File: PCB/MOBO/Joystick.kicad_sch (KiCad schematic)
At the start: 23 parts, among them J107 DTR, J107 MISO, J107 MOSI, J107 RXD, J107 SCK, J107 TXD, SW301 RS Button, SW302 LS Button, SW303 DPAD Right, SW304 DPAD Left, SW306 B Button, SW307 A Button, SW308 DPAD Down, SW309 DPAD Up, U301 ATmega328PB-M, Y301 YABM11-16.000MHZ-12-B1U-T

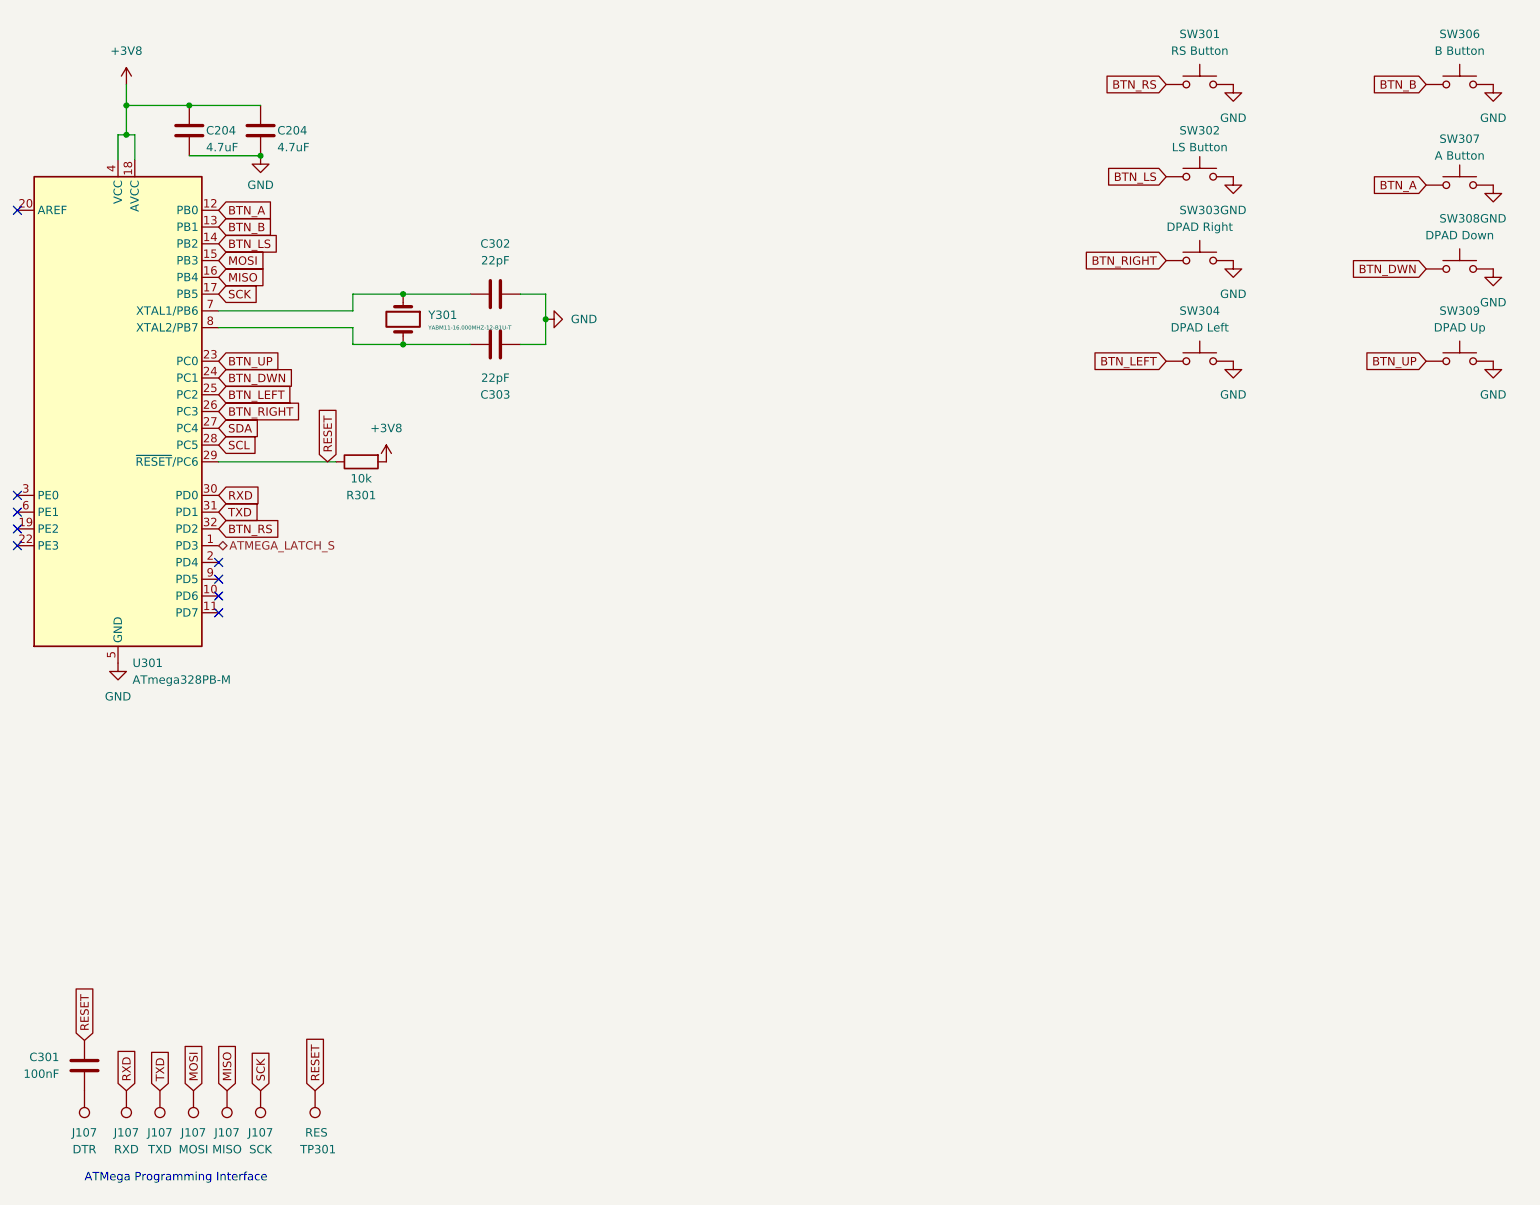
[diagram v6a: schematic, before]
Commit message: Started pcb traces
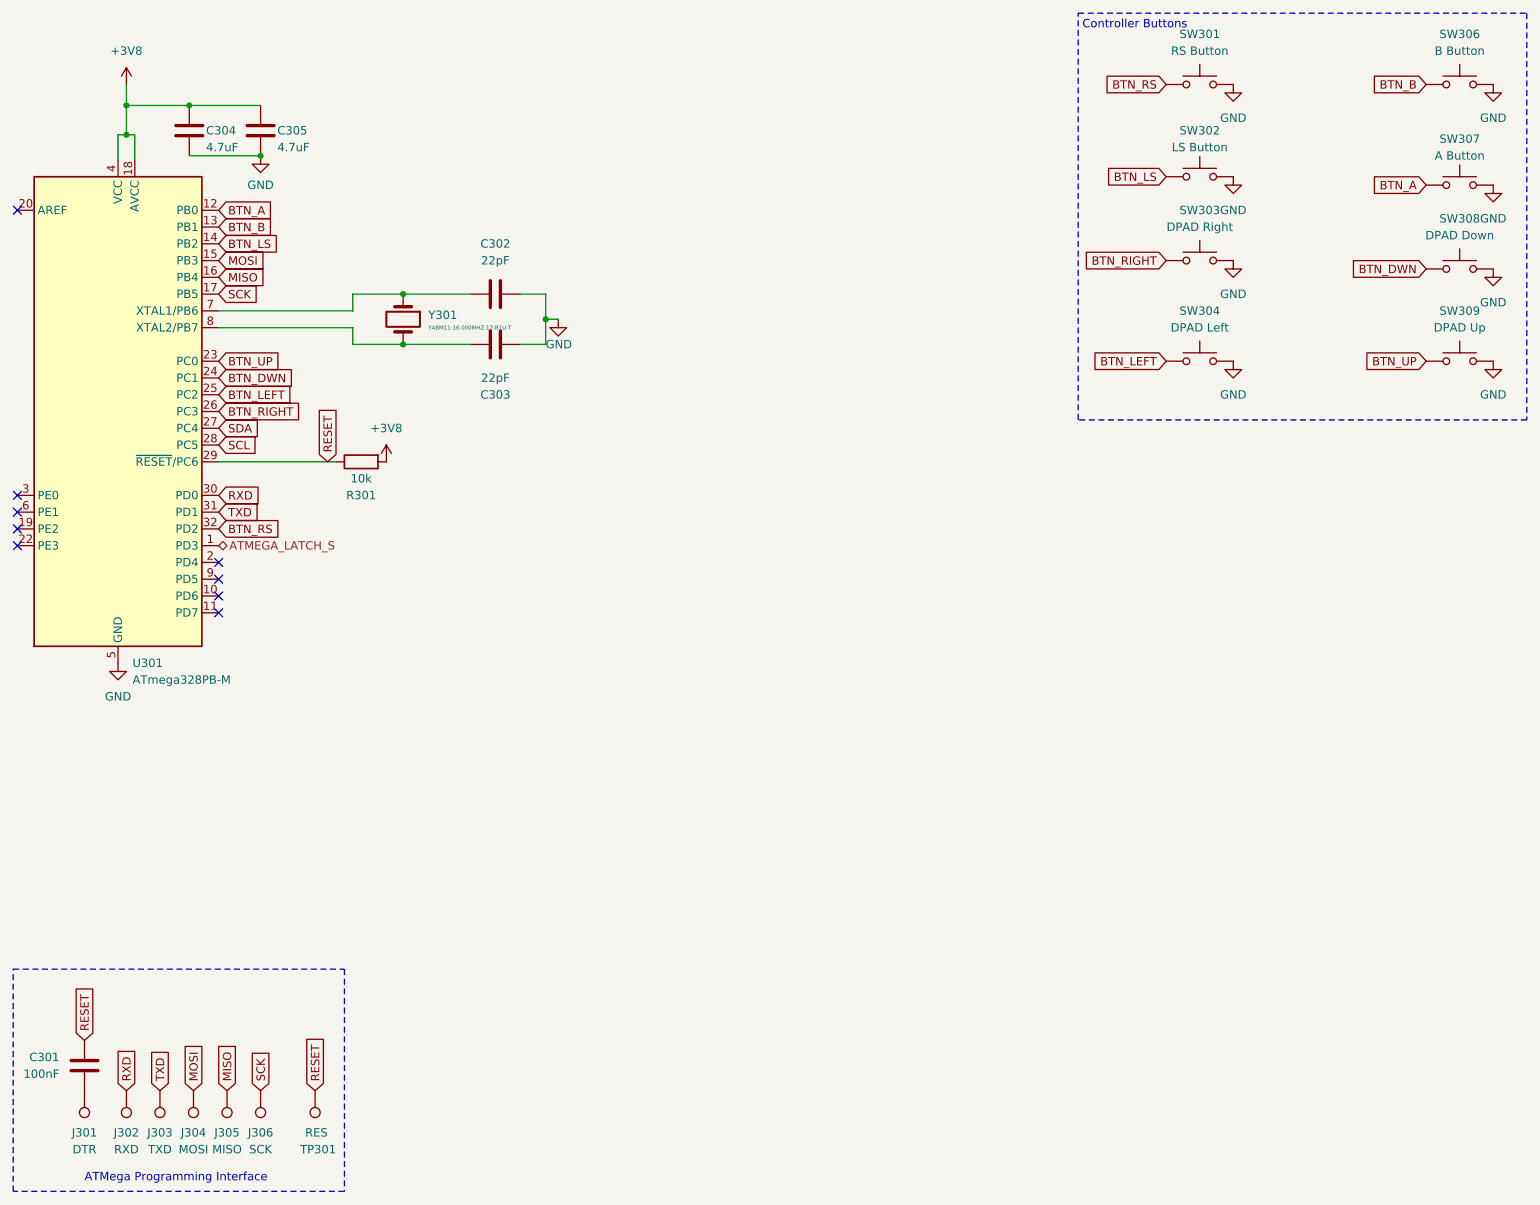
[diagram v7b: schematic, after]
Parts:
- renumbered C204 to C304, C204 to C305, J107 to J301, J107 to J302, J107 to J303, J107 to J304, J107 to J305, J107 to J306
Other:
- note added: "Controller Buttons"
- title: (none) -> ATMega & Buttons
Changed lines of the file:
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@@
 (kicad_sch (version 20230121) (generator eeschema)
   (paper "A4")
+  (title_block
+    (title "ATMega & Buttons")
+    (date "2023-06-06")
+    (rev "0.5")
+    (comment 1 "Repo: https://github.com/ilnerdchuck/GBA-SPi")
+  )
   (junction (at 78.74 64.77) (diameter 0) (color 0 0 0 0)
   )
@@
     (stroke (width 0) (type default))
   )
+  (wire (pts (xy 102.235 60.96) (xy 100.33 60.96))
+    (stroke (width 0) (type default))
+  )
   (wire (pts (xy 100.33 60.96) (xy 100.33 64.77))
     (stroke (width 0) (type default))
@@
     (stroke (width 0) (type default))
   )
+  (rectangle (start 180.975 14.605) (end 248.92 76.2)
+    (stroke (width 0) (type dash_dot_dot))
+    (fill (type none))
+  )
+  (rectangle (start 19.685 159.385) (end 69.85 193.04)
+    (stroke (width 0) (type dash_dot_dot))
+    (fill (type none))
+  )
   (text "ATMega Programming Interface\n" (at 30.48 191.77 0)
+    (effects (font (size 1.27 1.27)) (justify left bottom))
+  )
+  (text "Controller Buttons\n" (at 181.61 17.145 0)
     (effects (font (size 1.27 1.27)) (justify left bottom))
   )
@@
     )
   )
-  (symbol (lib_id "power:GND") (at 100.33 60.96 90) (unit 1)
-    (in_bom yes) (on_board yes) (dnp no) (fields_autoplaced)
-    (property "Reference" "#PWR0302" (at 106.68 60.96 0)
-      (effects (font (size 1.27 1.27)) hide)
-    )
-    (property "Value" "GND" (at 104.14 60.96 90)
-      (effects (font (size 1.27 1.27)) (justify right))
-    )
-    (property "Footprint" "" (at 100.33 60.96 0)
-      (effects (font (size 1.27 1.27)) hide)
-    )
-    (property "Datasheet" "" (at 100.33 60.96 0)
+  (symbol (lib_id "power:GND") (at 102.235 60.96 0) (unit 1)
+    (in_bom yes) (on_board yes) (dnp no)
+    (property "Reference" "#PWR0302" (at 102.235 67.31 0)
+      (effects (font (size 1.27 1.27)) hide)
+    )
+    (property "Value" "GND" (at 100.33 64.77 0)
+      (effects (font (size 1.27 1.27)) (justify left))
+    )
+    (property "Footprint" "" (at 102.235 60.96 0)
+      (effects (font (size 1.27 1.27)) hide)
+    )
+    (property "Datasheet" "" (at 102.235 60.96 0)
       (effects (font (size 1.27 1.27)) hide)
     )
@@
   (symbol (lib_id "Connector:TestPoint") (at 30.48 177.8 180) (unit 1)
     (in_bom yes) (on_board yes) (dnp no)
-    (property "Reference" "J107" (at 30.48 184.15 0)
+    (property "Reference" "J301" (at 30.48 184.15 0)
       (effects (font (size 1.27 1.27)))
     )
@@
     (instances
       (project "MOBO"
-        (path "/2d62a3c1-c4f2-4921-9f6b-8dc8aef69d64"
-          (reference "J107") (unit 1)
-        )
         (path "/2d62a3c1-c4f2-4921-9f6b-8dc8aef69d64/7ca0e1b4-2467-452a-8d82-c598e33fab6f"
           (reference "J301") (unit 1)
@@
   (symbol (lib_id "Device:C") (at 46.355 32.385 0) (unit 1)
     (in_bom yes) (on_board yes) (dnp no)
-    (property "Reference" "C204" (at 48.895 32.385 0)
+    (property "Reference" "C304" (at 48.895 32.385 0)
       (effects (font (size 1.27 1.27)) (justify left))
     )
@@
     (instances
       (project "MOBO"
-        (path "/2d62a3c1-c4f2-4921-9f6b-8dc8aef69d64/968b581c-59b8-4e39-ae9d-82f589704db7"
-          (reference "C204") (unit 1)
-        )
         (path "/2d62a3c1-c4f2-4921-9f6b-8dc8aef69d64/7ca0e1b4-2467-452a-8d82-c598e33fab6f"
           (reference "C304") (unit 1)
@@
   (symbol (lib_id "Connector:TestPoint") (at 57.15 177.8 180) (unit 1)
     (in_bom yes) (on_board yes) (dnp no)
-    (property "Reference" "J107" (at 57.15 184.15 0)
+    (property "Reference" "J306" (at 57.15 184.15 0)
       (effects (font (size 1.27 1.27)))
     )
@@
     (instances
       (project "MOBO"
-        (path "/2d62a3c1-c4f2-4921-9f6b-8dc8aef69d64"
-          (reference "J107") (unit 1)
-        )
         (path "/2d62a3c1-c4f2-4921-9f6b-8dc8aef69d64/7ca0e1b4-2467-452a-8d82-c598e33fab6f"
           (reference "J306") (unit 1)
@@
   (symbol (lib_id "Connector:TestPoint") (at 41.91 177.8 180) (unit 1)
     (in_bom yes) (on_board yes) (dnp no)
-    (property "Reference" "J107" (at 41.91 184.15 0)
+    (property "Reference" "J303" (at 41.91 184.15 0)
       (effects (font (size 1.27 1.27)))
     )
@@
     (instances
       (project "MOBO"
-        (path "/2d62a3c1-c4f2-4921-9f6b-8dc8aef69d64"
-          (reference "J107") (unit 1)
-        )
         (path "/2d62a3c1-c4f2-4921-9f6b-8dc8aef69d64/7ca0e1b4-2467-452a-8d82-c598e33fab6f"
           (reference "J303") (unit 1)
@@
   (symbol (lib_id "Device:C") (at 57.15 32.385 0) (unit 1)
     (in_bom yes) (on_board yes) (dnp no)
-    (property "Reference" "C204" (at 59.69 32.385 0)
+    (property "Reference" "C305" (at 59.69 32.385 0)
       (effects (font (size 1.27 1.27)) (justify left))
     )
@@
     (instances
       (project "MOBO"
-        (path "/2d62a3c1-c4f2-4921-9f6b-8dc8aef69d64/968b581c-59b8-4e39-ae9d-82f589704db7"
-          (reference "C204") (unit 1)
-        )
         (path "/2d62a3c1-c4f2-4921-9f6b-8dc8aef69d64/7ca0e1b4-2467-452a-8d82-c598e33fab6f"
           (reference "C305") (unit 1)
@@
   (symbol (lib_id "Connector:TestPoint") (at 36.83 177.8 180) (unit 1)
     (in_bom yes) (on_board yes) (dnp no)
-    (property "Reference" "J107" (at 36.83 184.15 0)
+    (property "Reference" "J302" (at 36.83 184.15 0)
       (effects (font (size 1.27 1.27)))
     )
@@
     (instances
       (project "MOBO"
-        (path "/2d62a3c1-c4f2-4921-9f6b-8dc8aef69d64"
-          (reference "J107") (unit 1)
-        )
         (path "/2d62a3c1-c4f2-4921-9f6b-8dc8aef69d64/7ca0e1b4-2467-452a-8d82-c598e33fab6f"
           (reference "J302") (unit 1)
@@
   (symbol (lib_id "Connector:TestPoint") (at 46.99 177.8 180) (unit 1)
     (in_bom yes) (on_board yes) (dnp no)
-    (property "Reference" "J107" (at 46.99 184.15 0)
+    (property "Reference" "J304" (at 46.99 184.15 0)
       (effects (font (size 1.27 1.27)))
     )
@@
     (instances
       (project "MOBO"
-        (path "/2d62a3c1-c4f2-4921-9f6b-8dc8aef69d64"
-          (reference "J107") (unit 1)
-        )
         (path "/2d62a3c1-c4f2-4921-9f6b-8dc8aef69d64/7ca0e1b4-2467-452a-8d82-c598e33fab6f"
           (reference "J304") (unit 1)
@@
   (symbol (lib_id "Connector:TestPoint") (at 52.07 177.8 180) (unit 1)
     (in_bom yes) (on_board yes) (dnp no)
-    (property "Reference" "J107" (at 52.07 184.15 0)
+    (property "Reference" "J305" (at 52.07 184.15 0)
       (effects (font (size 1.27 1.27)))
     )
@@
     (instances
       (project "MOBO"
-        (path "/2d62a3c1-c4f2-4921-9f6b-8dc8aef69d64"
-          (reference "J107") (unit 1)
-        )
         (path "/2d62a3c1-c4f2-4921-9f6b-8dc8aef69d64/7ca0e1b4-2467-452a-8d82-c598e33fab6f"
           (reference "J305") (unit 1)
